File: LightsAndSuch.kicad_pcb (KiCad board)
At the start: 4 copper layers, 67.3 x 76.8 mm, 75 parts, among them J1 Conn_01x02_Pin, J2 Conn_02x06_Odd_Even, J8 Conn_02x06_Odd_Even, P1 USB_C_Plug_USB2.0, Q1 AO3400A, Q2 AO3400A, Q3 AO3400A, Q4 AO3400A, Q5 AO3400A, U1 RP2040, U2 MAX98357A, U3 TPS54202DDC, U4 LM3940IMP-3.3, U5 CD4081BM, U6 LM555xM, U7 LM555xM, U8 W25Q128JVS, U9 NCP1117-3.3_SOT223

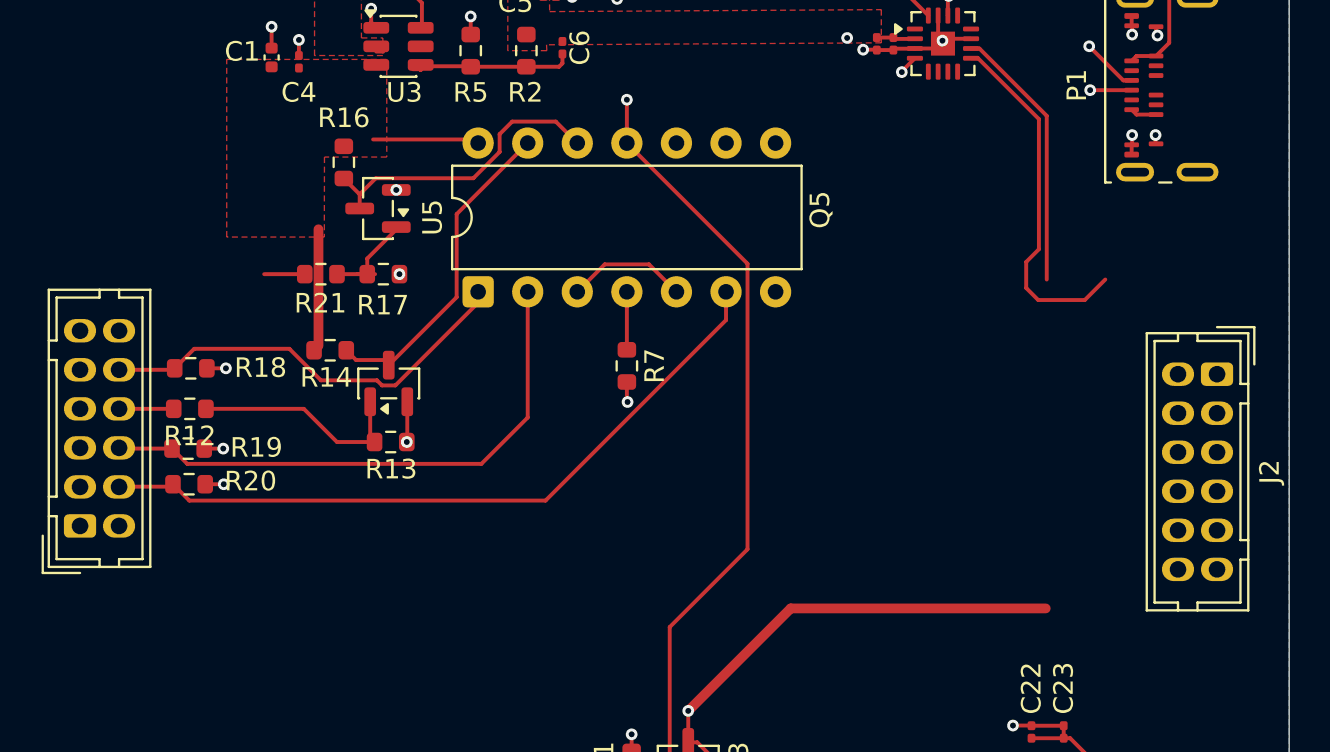
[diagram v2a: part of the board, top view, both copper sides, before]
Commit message: changed from global labels to net labels
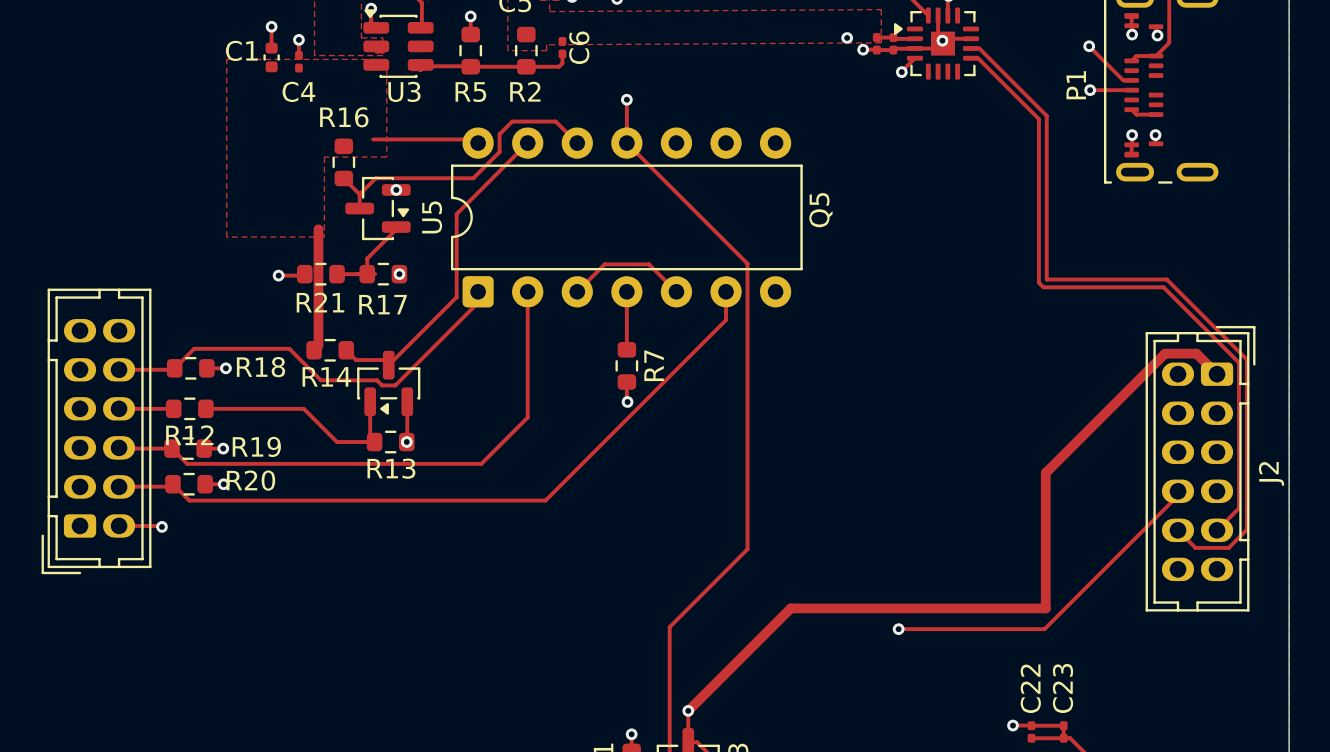
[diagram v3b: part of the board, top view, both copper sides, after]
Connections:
- C1 pad 1: FAULT_ANODE -> +12V
- C1 pad 2: OK_CATHODE -> GND
- C10 pad 2: OK_CATHODE -> GND
- C11 pad 2: OK_CATHODE -> GND
- C12 pad 2: OK_CATHODE -> GND
- C13 pad 2: OK_CATHODE -> GND
- C14 pad 2: OK_CATHODE -> GND
- C15 pad 2: OK_CATHODE -> GND
- C16 pad 2: OK_CATHODE -> GND
- C17 pad 1: OK_CATHODE -> GND
- C17 pad 2: LS2_P -> +5V
- C18 pad 1: OK_CATHODE -> GND
- C18 pad 2: LS2_P -> +5V
- C19 pad 1: LS2_P -> +5V
- C19 pad 2: LS2_P -> +5V
- C2 pad 1: LS2_P -> +5V
- C2 pad 2: LS2_P -> +5V
- C20 pad 2: OK_CATHODE -> GND
- C21 pad 1: OK_CATHODE -> GND
- C21 pad 2: LS2_P -> +5V
- C22 pad 1: LS2_P -> +5V
- C22 pad 2: LS2_P -> +5V
- C23 pad 1: LS2_P -> +5V
- C23 pad 2: LS2_P -> +5V
- C24 pad 1: LS2_P -> +5V
- C24 pad 2: LS2_P -> +5V
- C25 pad 1: LS2_P -> +5V
- C25 pad 2: LS2_P -> +5V
- C26 pad 1: LS2_P -> +5V
- C26 pad 2: FAULT_ANODE -> +12V
- C27 pad 1: OK_CATHODE -> GND
- C28 pad 2: OK_CATHODE -> GND
- C29 pad 2: OK_CATHODE -> GND
- C3 pad 1: LS2_P -> +5V
- C3 pad 2: OK_CATHODE -> GND
- C30 pad 2: OK_CATHODE -> GND
- C31 pad 2: OK_CATHODE -> GND
- C32 pad 2: OK_CATHODE -> GND
- C33 pad 2: OK_CATHODE -> GND
- C4 pad 1: FAULT_ANODE -> +12V
- C4 pad 2: OK_CATHODE -> GND
- C5 pad 1: LS2_P -> +5V
- C5 pad 2: OK_CATHODE -> GND
- C6 pad 1: LS2_P -> +5V
- C7 pad 1: LS2_P -> +5V
- C7 pad 2: OK_CATHODE -> GND
- C8 pad 2: OK_CATHODE -> GND
- C9 pad 1: OK_CATHODE -> GND
- J1 pad 1: OK_CATHODE -> GND
- J2 pad 1: LS1_P -> +12V
- J2 pad 10: FAULT_CATHODE -> /LS1_N
- J2 pad 2: LS1_N -> /FAULT_N
- J2 pad 3: LS2_P -> +5V
- J2 pad 4: LS2_n -> /LS2_N
- J2 pad 5: LS2_P -> +12V
- J2 pad 6: LS2_n -> GND
- J2 pad 7: FAULT_ANODE -> +5V
- J2 pad 8: OK_CATHODE -> /LS2_N
- J2 pad 9: FAULT_ANODE -> /LS1_P
- J8 pad 1: OK_CATHODE -> GND
- J8 pad 11: OK_CATHODE -> GND
- J8 pad 3: OK_CATHODE -> GND
- J8 pad 5: OK_CATHODE -> GND
- J8 pad 7: OK_CATHODE -> GND
- J8 pad 9: OK_CATHODE -> GND
- L1 pad 2: LS2_P -> +5V
- P1 pad A1: OK_CATHODE -> GND
- P1 pad A12: OK_CATHODE -> GND
- P1 pad B1: OK_CATHODE -> GND
- P1 pad B12: OK_CATHODE -> GND
- P1 pad S1: OK_CATHODE -> GND
- Q1 pad 2: OK_CATHODE -> GND
- Q1 pad 3: LS2_n -> /LS2_N
- Q2 pad 3: FAULT_CATHODE -> /FAULT_N
- Q3 pad 2: OK_CATHODE -> GND
- Q3 pad 3: FAULT_ANODE -> +12V
- Q4 pad 2: OK_CATHODE -> GND
- Q5 pad 2: OK_CATHODE -> GND
- R1 pad 1: LS2_P -> +5V
- R11 pad 1: OK_CATHODE -> GND
- R13 pad 2: OK_CATHODE -> GND
- R14 pad 1: FAULT_ANODE -> +12V
- R15 pad 1: OK_CATHODE -> GND
- R16 pad 1: FAULT_ANODE -> +12V
- R17 pad 2: OK_CATHODE -> GND
- R18 pad 1: OK_CATHODE -> GND
- R19 pad 1: OK_CATHODE -> GND
- R2 pad 1: LS2_P -> +5V
- R20 pad 1: OK_CATHODE -> GND
- R3 pad 1: OK_CATHODE -> GND
- R4 pad 2: OK_CATHODE -> GND
- R5 pad 2: OK_CATHODE -> GND
- R6 pad 2: OK_CATHODE -> GND
- R9 pad 1: LS2_P -> +5V
- U1 pad 57: OK_CATHODE -> GND
- U2 pad 10: LS1_N -> /LS1_N
- U2 pad 11: OK_CATHODE -> GND
- U2 pad 15: OK_CATHODE -> GND
- U2 pad 17: OK_CATHODE -> GND
- U2 pad 2: LS2_P -> +5V
- U2 pad 3: OK_CATHODE -> GND
- U2 pad 7: LS2_P -> +5V
- U2 pad 8: LS2_P -> +5V
- U2 pad 9: LS1_P -> /LS1_P
- U3 pad 1: OK_CATHODE -> GND
- U3 pad 3: FAULT_ANODE -> +12V
- U4 pad 1: LS2_P -> +5V
- U4 pad 2: OK_CATHODE -> GND
- U5 pad 14: FAULT_ANODE -> +12V
- U5 pad 7: OK_CATHODE -> GND
- U6 pad 1: OK_CATHODE -> GND
- U6 pad 4: OK_CATHODE -> GND
- U6 pad 6: LS2_P -> +5V
- U6 pad 8: LS2_P -> +5V
- U7 pad 1: OK_CATHODE -> GND
- U7 pad 8: LS2_P -> +5V
- U8 pad 4: OK_CATHODE -> GND
- U9 pad 1: OK_CATHODE -> GND
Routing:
- net +12V: track 0.00 -> 98.2 mm, vias 0 -> 1
- net LS2_P: track 88.8 -> 0.00 mm, vias 4 -> 0
- net +5V: track 0.00 -> 88.8 mm, vias 0 -> 4
- net FAULT_ANODE: track 79.5 -> 0.00 mm, vias 1 -> 0
- net /LS2_N: track 0.00 -> 77.7 mm, vias 0 -> 2
- net LS2_n: track 70.9 -> 0.00 mm, vias 1 -> 0
- net /FAULT_N: track 0.00 -> 58.7 mm, vias 0 -> 1
- net OK_CATHODE: track 52.5 -> 0.00 mm, vias 56 -> 0
- net GND: track 0.00 -> 52.5 mm, vias 0 -> 56
- net FAULT_CATHODE: track 45.1 -> 0.00 mm, vias 1 -> 0
- net /LS1_N: track 0.00 -> 38.7 mm
- net /LS1_P: track 0.00 -> 34.2 mm
- net IMD_Fault: track 2.08 -> 20.6 mm, vias 0 -> 2
- net LS1_P: track 18.4 -> 0.00 mm
- net (no net): track 17.2 -> 0.00 mm
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- added copper zone on F.Cu, net +12V
- added copper zone on F.Cu, net +5V
- added copper zone on B.Cu, net GND
- added copper zone on In1.Cu, net GND
- added copper zone on In2.Cu, net GND
- removed copper zone on F.Cu, net FAULT_ANODE
- removed copper zone on F.Cu, net LS2_P
- removed copper zone on B.Cu, net OK_CATHODE
- removed copper zone on In1.Cu, net OK_CATHODE
- removed copper zone on In2.Cu, net OK_CATHODE

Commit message: some updates
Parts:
- moved R6 34.0 mm to (88.5, 114.5), turned to 180 degrees
- moved R15 2.34 mm to (88.8, 136.0)
- moved C31 1.92 mm to (103.2, 80.6)
- moved Q2 1.75 mm to (88.5, 140.6)
- moved R7 1.20 mm to (90.8, 111.8)
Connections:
- J8 pad 12: /VIN -> IMD_Fault
- J8 pad 2: IMD_Fault -> /VIN
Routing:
- net /LS2_N: track 77.7 -> 23.3 mm
- net +5V: track 88.8 -> 50.1 mm, vias 4 -> 3
- net +3.3V: track 63.6 -> 37.6 mm
- net Trigger: track 95.4 -> 73.7 mm
- net IMD_Fault: track 20.6 -> 10.7 mm, vias 2 -> 1
- net Net-(Q2-G): track 6.14 -> 0.35 mm
- net Net-(U1-GPIO12): track 0.00 -> 5.73 mm, vias 0 -> 2
- net /QSPI_SDO: track 17.5 -> 13.2 mm
- net /QSPI_SCLK: track 16.1 -> 12.4 mm
- net /USB_D+: track 21.1 -> 18.4 mm
- net Fault: track 49.5 -> 47.0 mm
- net /QSPI_SD2: track 14.0 -> 15.9 mm
- net /FAULT_N: track 58.7 -> 57.6 mm
- net Net-(U5-K): track 2.97 -> 1.91 mm
- net Net-(Q2-S): track 16.1 -> 17.0 mm
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- removed copper zone on B.Cu, net GND

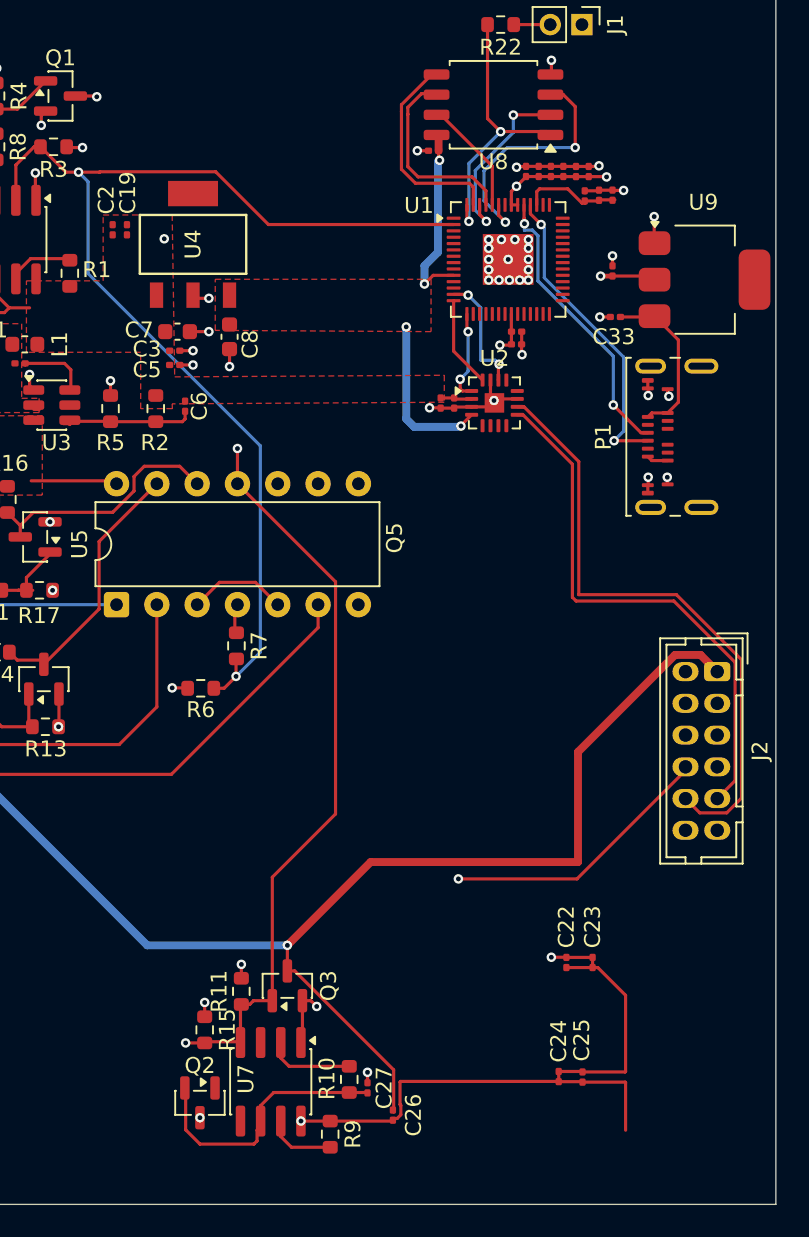
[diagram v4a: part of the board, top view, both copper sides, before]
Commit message: some decoup caps
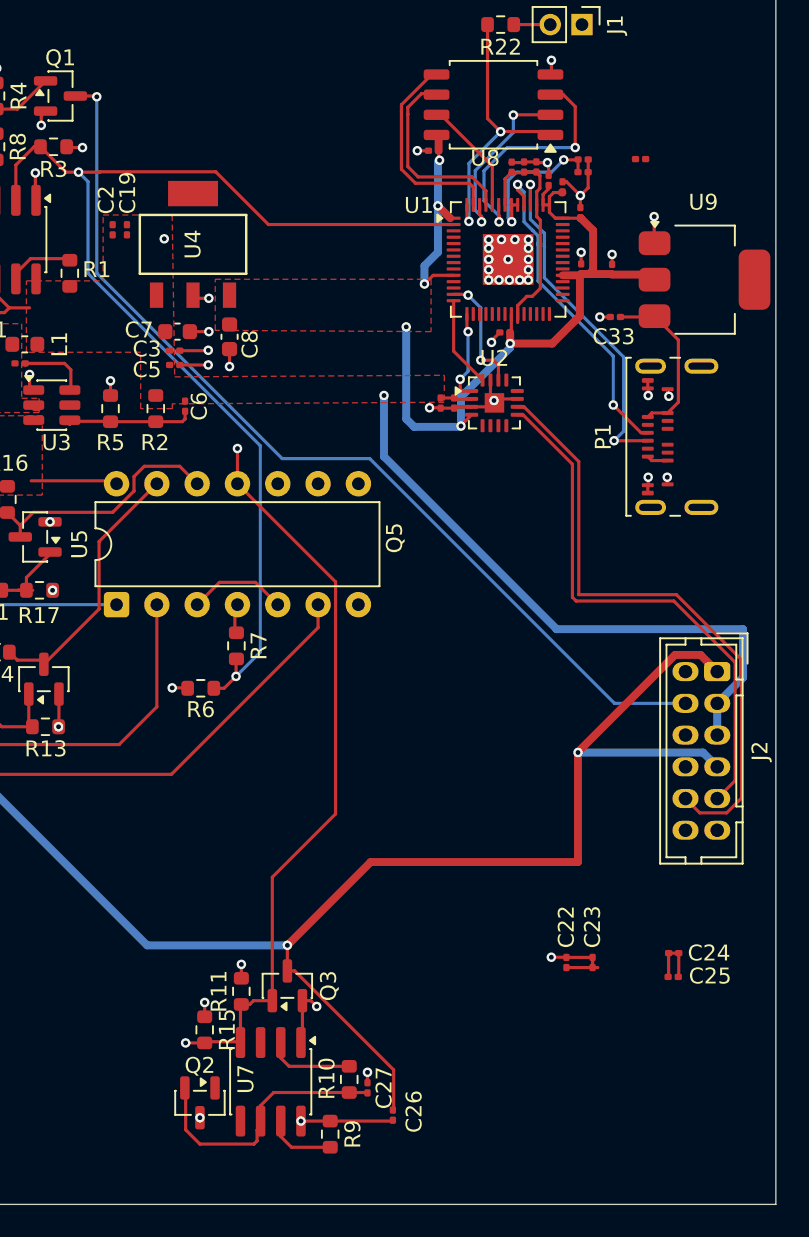
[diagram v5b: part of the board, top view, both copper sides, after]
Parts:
- moved C24 10.6 mm to (118.4, 131.2), turned to 0 degrees
- moved C25 8.51 mm to (118.3, 132.7), turned to 0 degrees
- moved C15 6.26 mm to (112.5, 88.0), turned to 90 degrees
- moved C29 5.12 mm to (109.7, 81.6)
- moved C30 5.05 mm to (108.9, 81.6)
- moved C28 4.94 mm to (108.2, 81.6)
- moved C16 4.30 mm to (112.5, 84.5)
- moved C13 3.36 mm to (116.3, 81.1), turned to 0 degrees
- moved C9 1.79 mm to (111.3, 82.9)
- moved C11 1.46 mm to (112.7, 81.2), turned to 0 degrees
- moved C14 0.74 mm to (107.7, 92.0), turned to 180 degrees
- moved C10 0.58 mm to (110.5, 82.5)
- moved C12 0.45 mm to (112.6, 82.0), turned to 0 degrees
- moved C32 0.09 mm to (114.5, 88.1)
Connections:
- J2 pad 5: +12V -> +5V
- J2 pad 7: +5V -> +12V
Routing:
- net /LS2_N: track 23.3 -> 61.2 mm, vias 2 -> 1
- net +3.3V: track 37.6 -> 67.6 mm
- net +5V: track 50.1 -> 60.0 mm, vias 3 -> 4
- net +12V: track 97.7 -> 106.9 mm, vias 2 -> 3
- net Net-(U1-VREG_VOUT): track 6.10 -> 14.6 mm
- net /USB_D+: track 18.4 -> 21.0 mm
- net /USB_D-: track 19.7 -> 22.2 mm
- net GND: track 53.3 -> 55.6 mm

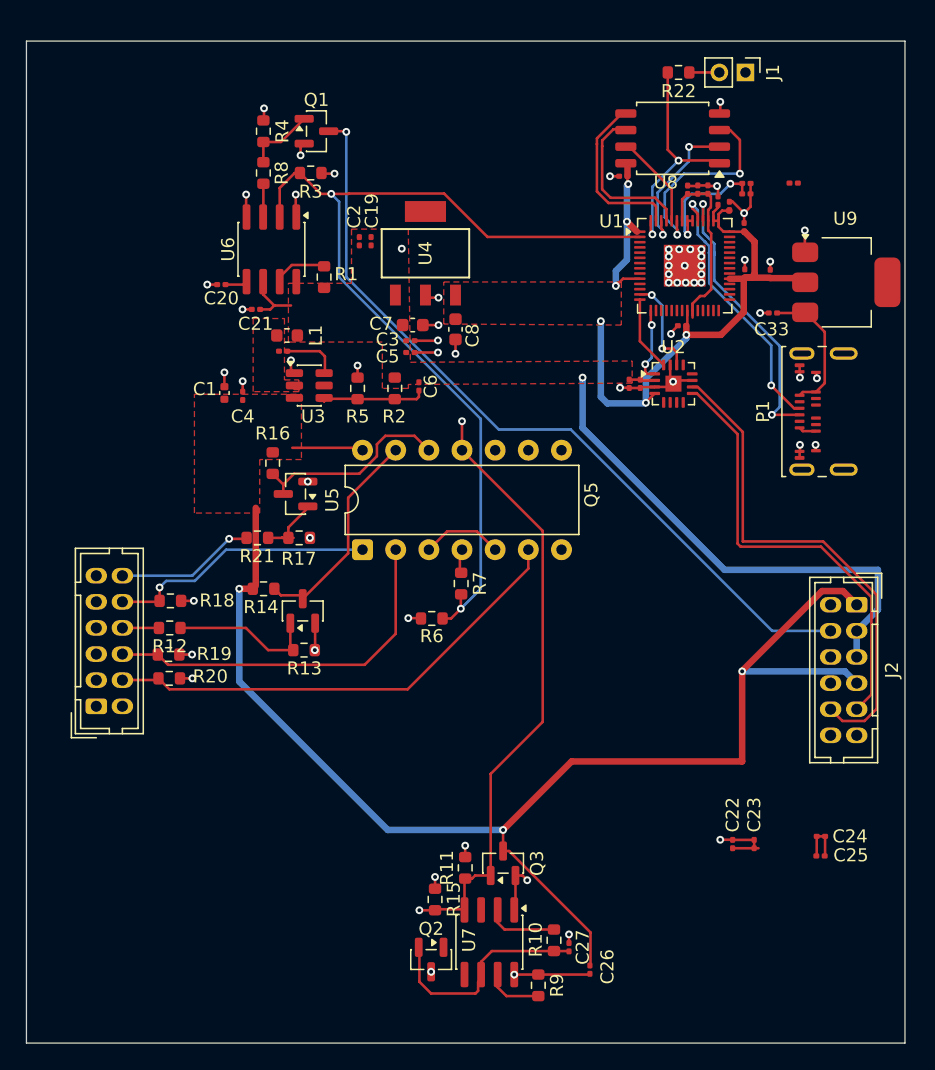
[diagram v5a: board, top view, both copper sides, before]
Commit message: passing DRC
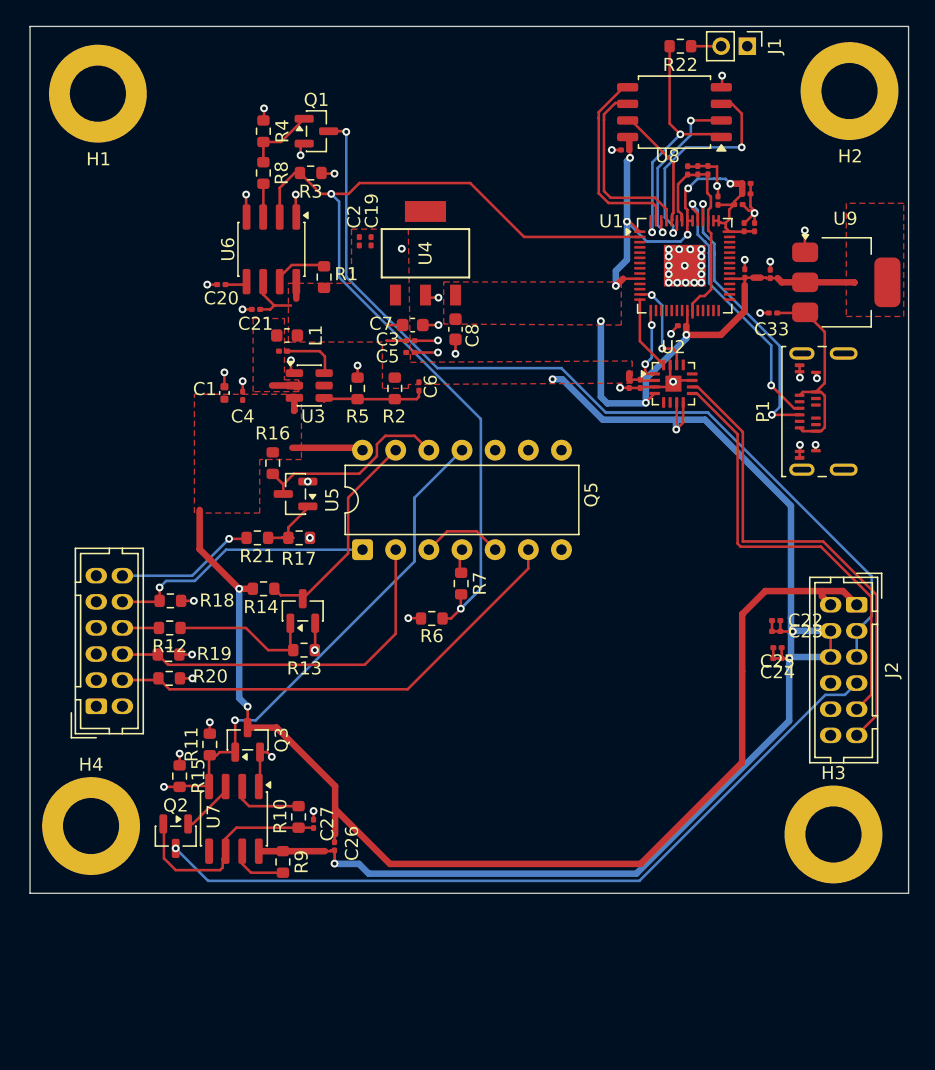
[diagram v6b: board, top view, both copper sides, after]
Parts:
- added H1: MountingHole_Pad, MountingHole:MountingHole_4.3mm_M4_DIN965_Pad, F.Cu at (63.0, 74.3)
- added H2: MountingHole_Pad, MountingHole:MountingHole_4.3mm_M4_DIN965_Pad, F.Cu at (120.5, 74.1)
- added H3: MountingHole_Pad, MountingHole:MountingHole_4.3mm_M4_DIN965_Pad, F.Cu at (119.3, 131.0)
- added H4: MountingHole_Pad, MountingHole:MountingHole_4.3mm_M4_DIN965_Pad, F.Cu at (62.5, 130.4)
- moved U7 21.7 mm to (73.4, 129.8)
- moved R15 21.7 mm to (69.2, 126.5)
- moved C26 21.7 mm to (81.1, 131.9)
- moved C27 21.7 mm to (79.5, 130.2)
- moved Q2 21.7 mm to (68.9, 131.2)
- moved Q3 21.7 mm to (74.4, 123.8)
- moved R10 21.7 mm to (78.3, 129.7)
- moved R11 21.7 mm to (71.5, 124.1)
- moved R9 21.7 mm to (77.1, 133.1)
- moved C22 17.4 mm to (114.9, 114.6), turned to 0 degrees
- moved C23 16.4 mm to (114.9, 115.5), turned to 0 degrees
- moved C25 16.3 mm to (115.0, 116.7), turned to 180 degrees
- moved C24 14.0 mm to (115.0, 117.5), turned to 180 degrees
- moved C13 4.51 mm to (113.3, 84.5), turned to 90 degrees
- moved J1 2.01 mm to (112.7, 70.6)
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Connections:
- J2 pad 10: /LS1_N -> GND
- J2 pad 11: unconnected-(J2-Pin_11-Pad11) -> /LS1_N
- J2 pad 2: /FAULT_N -> +12V
- J2 pad 3: +5V -> /LS2_N
- J2 pad 4: /LS2_N -> +5V
- J2 pad 5: +5V -> /LS2_N
- J2 pad 6: GND -> +5V
- J2 pad 7: +12V -> /FAULT_N
- J2 pad 8: /LS2_N -> unconnected-(J2-Pin_8-Pad8)
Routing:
- net +5V: track 60.0 -> 116.6 mm, vias 4 -> 6
- net +3.3V: track 67.6 -> 78.2 mm, vias 8 -> 9
- net +12V: track 106.9 -> 98.0 mm, vias 3 -> 2
- net /LS2_N: track 61.2 -> 69.0 mm
- net Fault: track 47.0 -> 39.2 mm
- net GND: track 55.6 -> 61.8 mm
- net Net-(U9-VI): track 11.9 -> 15.9 mm
- net Net-(Q2-G): track 0.35 -> 4.26 mm
- net Net-(U1-VREG_VOUT): track 14.6 -> 17.8 mm
- net /QSPI_SD3: track 7.29 -> 9.36 mm
- net /QSPI_SCLK: track 12.4 -> 14.3 mm
- net /QSPI_SDO: track 13.2 -> 15.1 mm
- net /FAULT_N: track 57.6 -> 59.5 mm
- net /QSPI_SD2: track 15.5 -> 17.3 mm
- net /QSPI_SS: track 17.9 -> 19.6 mm
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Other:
- board size 67.3 x 76.8 mm -> 67.3 x 66.4 mm
- rule pad_to_mask_clearance: 0 -> 0.0508
